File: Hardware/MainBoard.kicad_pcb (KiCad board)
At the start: 2 copper layers, 100 x 40 mm, 35 parts, among them J1 UPDI, J2 UART, J3 NMEA, J4 Vin, Q1 S8050, U1 HV5530, U2 HV5530, U3 ATtiny1606-S, U4 L78M05ABDT-TR

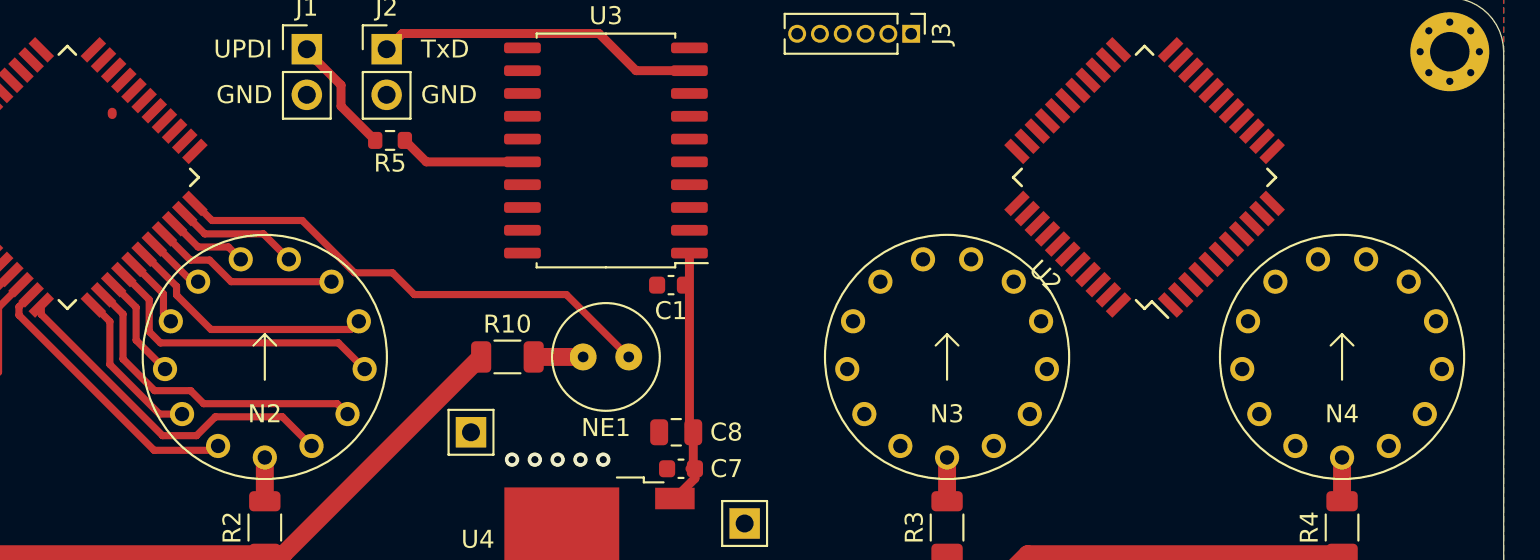
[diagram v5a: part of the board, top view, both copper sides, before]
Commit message: Routed right nixies
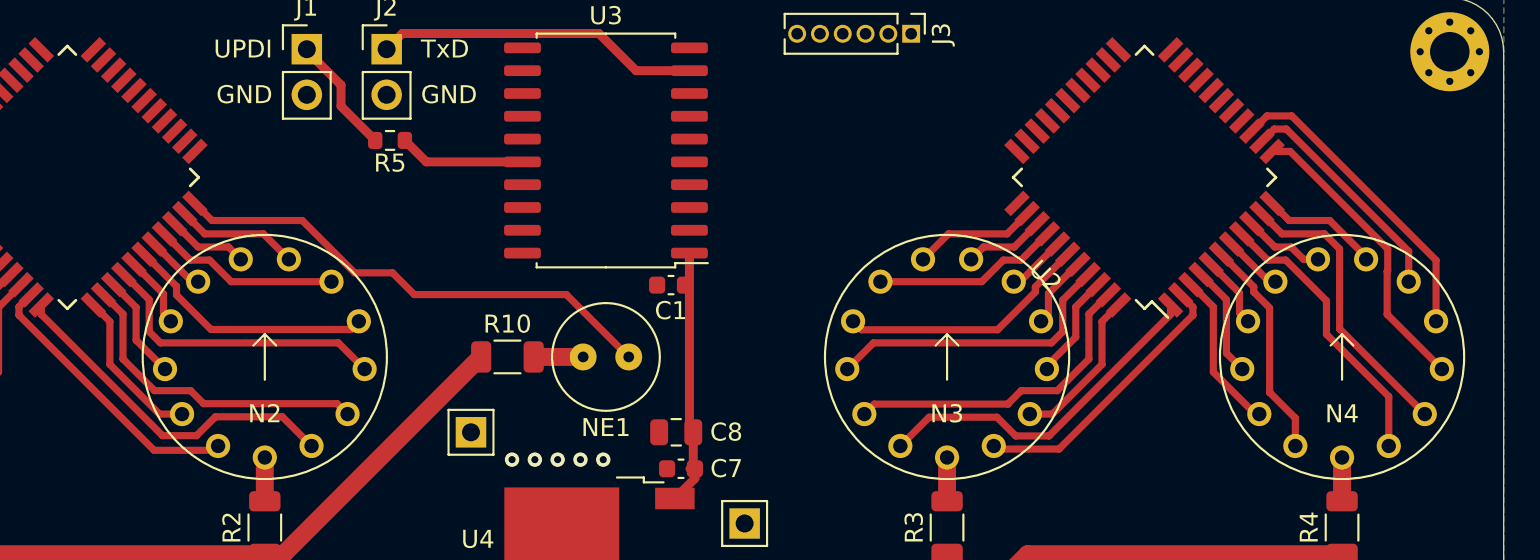
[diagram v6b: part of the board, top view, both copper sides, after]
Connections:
- U2 pad 1: /NixieTubes/N4_3 -> /NixieTubes/N3_L
- U2 pad 10: /NixieTubes/N3_7 -> /NixieTubes/N4_0
- U2 pad 11: /NixieTubes/N3_8 -> /NixieTubes/N4_6
- U2 pad 12: /NixieTubes/N3_9 -> /NixieTubes/N4_9
- U2 pad 13: /NixieTubes/N3_0 -> /NixieTubes/N4_7
- U2 pad 14: /NixieTubes/N3_R -> /NixieTubes/N4_8
- U2 pad 15: /NixieTubes/N3_L -> Net-(U2-Pad15)
- U2 pad 16: /NixieTubes/N3_1 -> Net-(U2-Pad16)
- U2 pad 17: /NixieTubes/N3_2 -> Net-(U2-Pad17)
- U2 pad 18: /NixieTubes/N3_3 -> Net-(U2-Pad18)
- U2 pad 2: /NixieTubes/N4_4 -> /NixieTubes/N3_R
- U2 pad 3: /NixieTubes/N4_5 -> /NixieTubes/N4_1
- U2 pad 35: Net-(U2-Pad35) -> /NixieTubes/N3_5
- U2 pad 36: Net-(U2-Pad36) -> /NixieTubes/N3_6
- U2 pad 37: Net-(U2-Pad37) -> /NixieTubes/N3_4
- U2 pad 38: /NixieTubes/N4_8 -> /NixieTubes/N3_7
- U2 pad 39: /NixieTubes/N4_9 -> /NixieTubes/N3_3
- U2 pad 4: /NixieTubes/N4_6 -> /NixieTubes/N4_2
- U2 pad 40: /NixieTubes/N4_0 -> /NixieTubes/N3_8
- U2 pad 41: /NixieTubes/N4_R -> /NixieTubes/N3_2
- U2 pad 42: /NixieTubes/N4_L -> /NixieTubes/N3_9
- U2 pad 43: /NixieTubes/N4_1 -> /NixieTubes/N3_1
- U2 pad 44: /NixieTubes/N4_2 -> /NixieTubes/N3_0
- U2 pad 5: /NixieTubes/N4_7 -> /NixieTubes/N4_3
- U2 pad 6: Net-(U2-Pad6) -> /NixieTubes/N4_L
- U2 pad 7: /NixieTubes/N3_4 -> /NixieTubes/N4_4
- U2 pad 8: /NixieTubes/N3_5 -> /NixieTubes/N4_R
- U2 pad 9: /NixieTubes/N3_6 -> /NixieTubes/N4_5
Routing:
- net /NixieTubes/N3_L: track 0.00 -> 19.5 mm
- net /NixieTubes/N3_1: track 0.00 -> 17.8 mm
- net /NixieTubes/N4_8: track 0.00 -> 17.3 mm
- net /NixieTubes/N4_9: track 0.00 -> 16.7 mm
- net /NixieTubes/N3_2: track 0.00 -> 16.6 mm
- net /NixieTubes/N4_0: track 0.00 -> 16.3 mm
- net /NixieTubes/N4_R: track 0.00 -> 15.8 mm
- net /NixieTubes/N3_R: track 0.00 -> 15.7 mm
- net /NixieTubes/N3_3: track 0.00 -> 14.1 mm
- net /NixieTubes/N4_7: track 0.00 -> 13.0 mm
- net /NixieTubes/N4_L: track 0.00 -> 12.4 mm
- net /NixieTubes/N3_4: track 0.00 -> 10.4 mm
- net /NixieTubes/N4_1: track 0.00 -> 8.92 mm
- net /NixieTubes/N3_0: track 0.00 -> 8.86 mm
- net /NixieTubes/N3_5: track 0.00 -> 6.86 mm
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
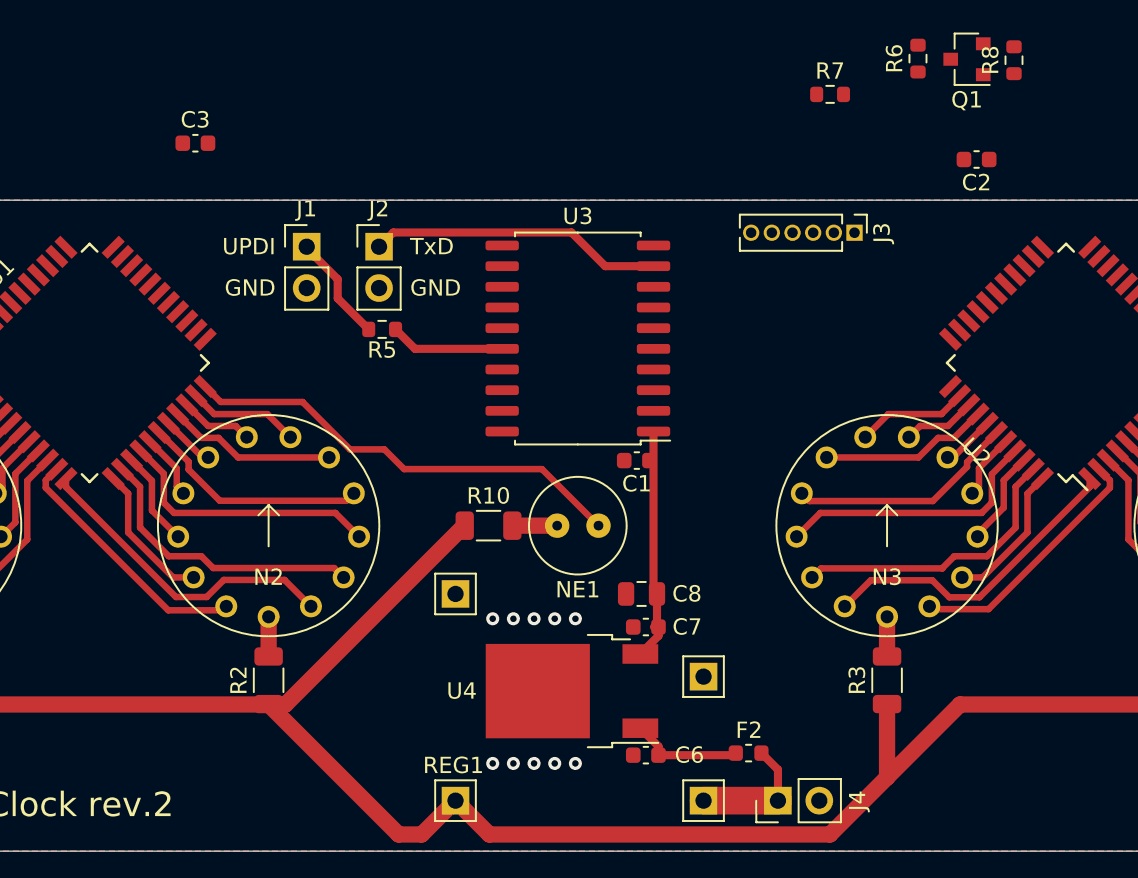
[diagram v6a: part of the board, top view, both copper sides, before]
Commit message: Finish routing connections
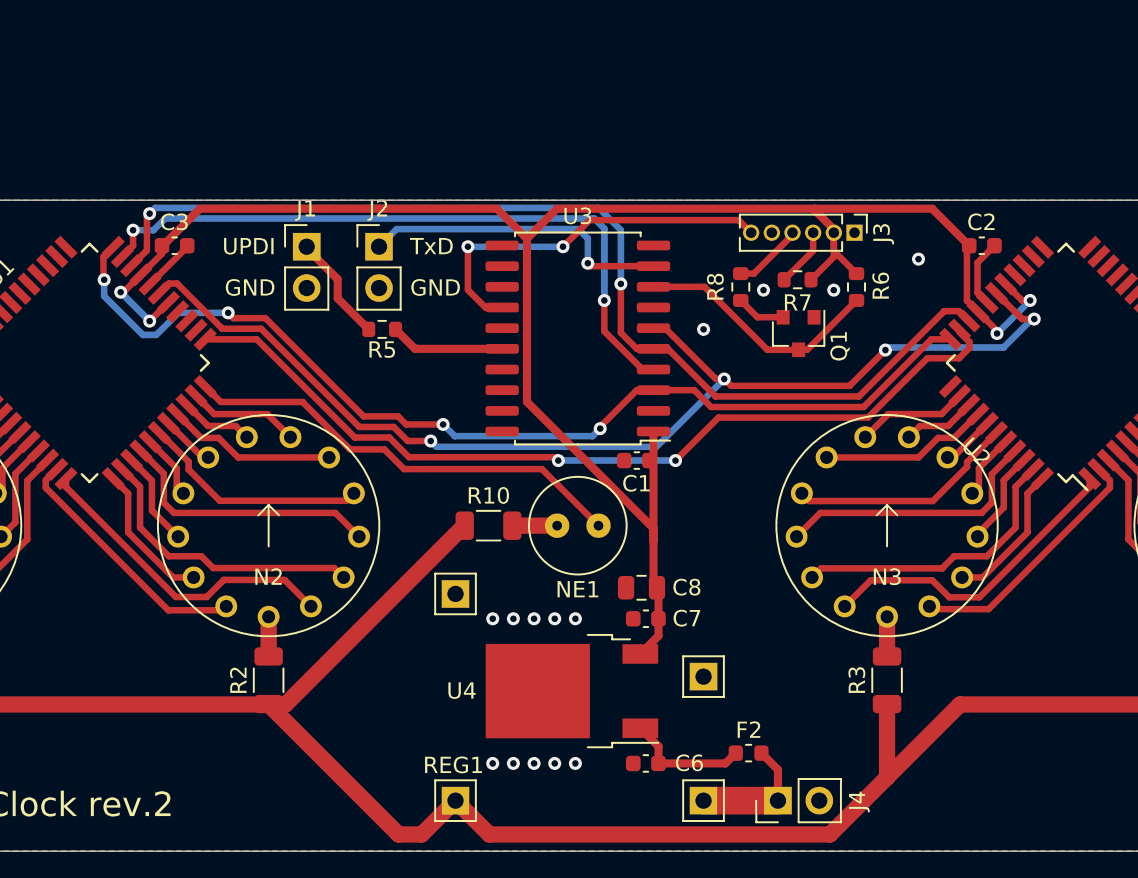
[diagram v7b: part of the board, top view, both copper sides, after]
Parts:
- moved R8 21.8 mm to (80.0, 25.3), turned to 270 degrees
- moved Q1 19.8 mm to (83.6, 28.2), turned to 270 degrees
- moved R6 14.5 mm to (87.1, 25.3), turned to 270 degrees
- moved R7 11.6 mm to (83.5, 24.9), turned to 180 degrees
- moved C3 6.43 mm to (45.2, 22.8)
- moved C2 5.31 mm to (94.8, 22.8), turned to 0 degrees
- moved C6 0.51 mm to (74.2, 54.6)
- moved C7 0.51 mm to (74.2, 45.7)
- moved C8 0.38 mm to (73.9, 43.8)
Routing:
- net +5V: track 14.3 -> 116.8 mm, vias 0 -> 4
- net NIX_CLK: track 0.00 -> 70.4 mm, vias 0 -> 4
- net NIX_LE: track 0.00 -> 65.1 mm, vias 0 -> 2
- net NIX_DIM: track 0.00 -> 64.0 mm, vias 0 -> 4
- net Net-(U1-Pad23): track 0.00 -> 54.2 mm, vias 0 -> 2
- net NIX_DATA: track 0.00 -> 41.7 mm, vias 0 -> 2
- net NMEA_SYNC: track 0.00 -> 23.6 mm, vias 0 -> 2
- net NMEA_RxD: track 0.00 -> 15.3 mm
- net GND: track 0.00 -> 7.47 mm, vias 10 -> 14
- net Net-(J3-Pad4): track 0.00 -> 4.30 mm
- net Net-(J3-Pad3): track 0.00 -> 3.63 mm
- net Net-(Q1-Pad2): track 0.00 -> 3.03 mm
- net UART_TxD: track 18.1 -> 19.2 mm, vias 0 -> 1
- net Net-(C6-Pad1): track 6.92 -> 7.82 mm

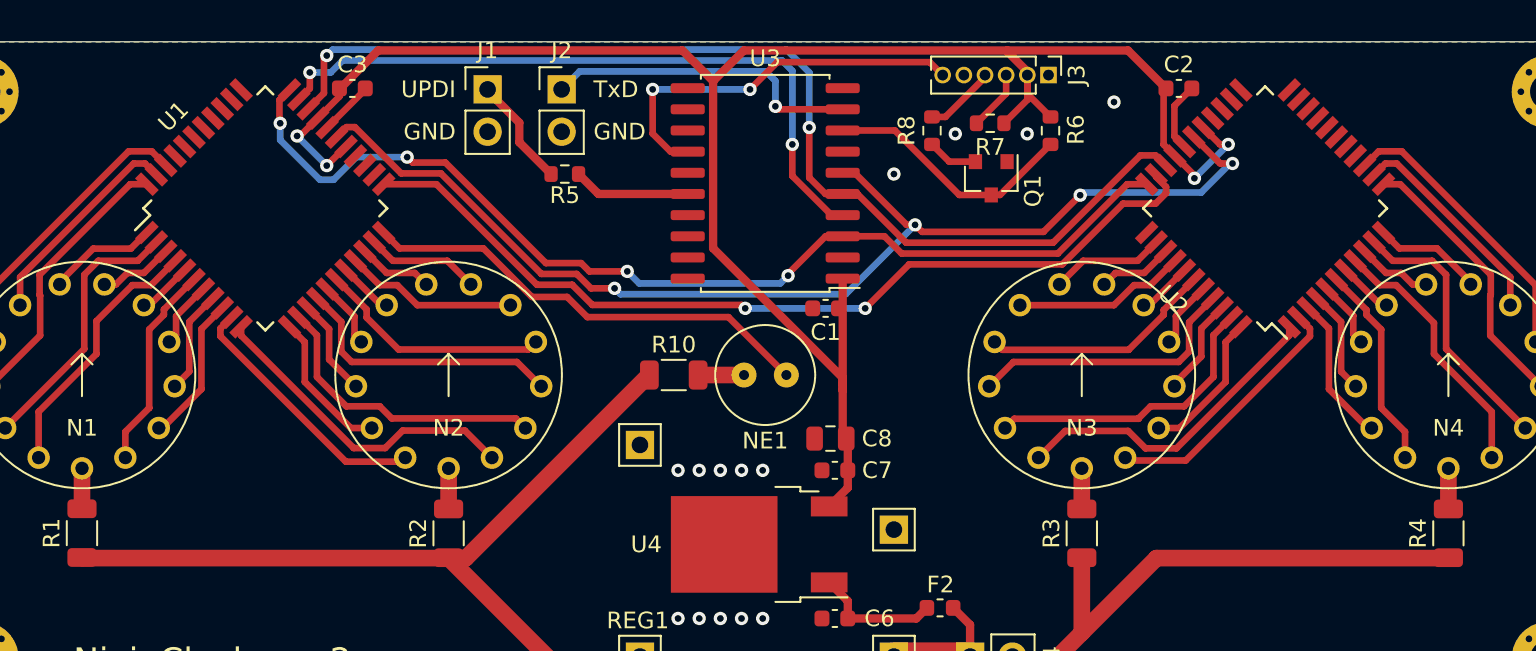
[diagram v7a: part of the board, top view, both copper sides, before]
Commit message: Add ground vias
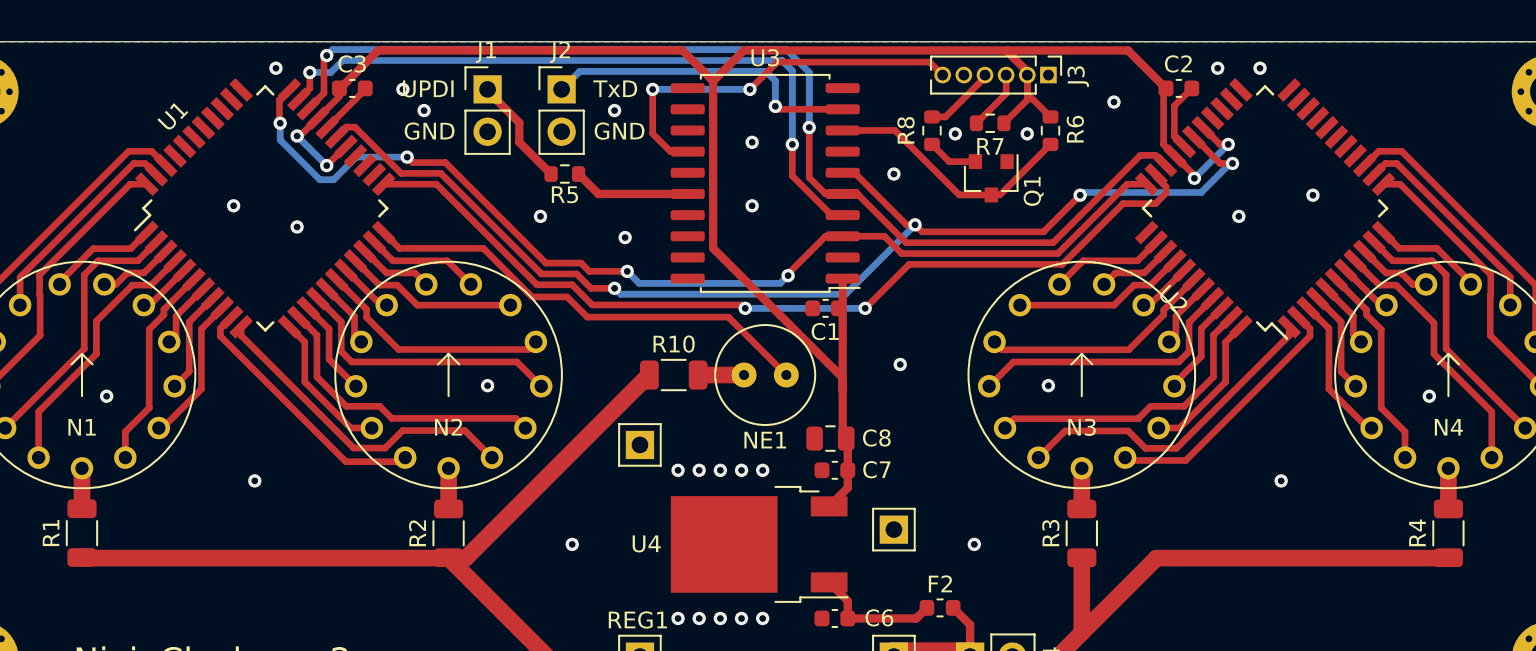
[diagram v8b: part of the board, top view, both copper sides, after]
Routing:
- net GND: vias 14 -> 37
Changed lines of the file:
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@@
     (thickness 1.6)
     (drawings 14)
-    (tracks 475)
+    (tracks 498)
     (zones 0)
     (modules 35)
@@
   (via (at 90.932 23.622) (size 0.8) (drill 0.4) (layers F.Cu B.Cu) (net 1))
   (via (at 77.724 27.94) (size 0.8) (drill 0.4) (layers F.Cu B.Cu) (net 1))
+  (via (at 69.215 26.035) (size 0.8) (drill 0.4) (layers F.Cu B.Cu) (net 1))
+  (via (at 69.215 29.845) (size 0.8) (drill 0.4) (layers F.Cu B.Cu) (net 1))
+  (via (at 61.595 31.75) (size 0.8) (drill 0.4) (layers F.Cu B.Cu) (net 1))
+  (via (at 56.515 30.48) (size 0.8) (drill 0.4) (layers F.Cu B.Cu) (net 1))
+  (via (at 60.96 24.13) (size 0.8) (drill 0.4) (layers F.Cu B.Cu) (net 1))
+  (via (at 49.53 24.13) (size 0.8) (drill 0.4) (layers F.Cu B.Cu) (net 1))
+  (via (at 38.1 29.845) (size 0.8) (drill 0.4) (layers F.Cu B.Cu) (net 1))
+  (via (at 41.91 31.115) (size 0.8) (drill 0.4) (layers F.Cu B.Cu) (net 1))
+  (via (at 98.425 30.48) (size 0.8) (drill 0.4) (layers F.Cu B.Cu) (net 1))
+  (via (at 102.87 29.21) (size 0.8) (drill 0.4) (layers F.Cu B.Cu) (net 1))
+  (via (at 109.855 41.275) (size 0.8) (drill 0.4) (layers F.Cu B.Cu) (net 1))
+  (via (at 86.995 40.64) (size 0.8) (drill 0.4) (layers F.Cu B.Cu) (net 1))
+  (via (at 53.34 40.64) (size 0.8) (drill 0.4) (layers F.Cu B.Cu) (net 1))
+  (via (at 30.48 41.275) (size 0.8) (drill 0.4) (layers F.Cu B.Cu) (net 1))
+  (via (at 39.37 46.355) (size 0.8) (drill 0.4) (layers F.Cu B.Cu) (net 1))
+  (via (at 100.965 46.355) (size 0.8) (drill 0.4) (layers F.Cu B.Cu) (net 1))
+  (via (at 82.55 50.165) (size 0.8) (drill 0.4) (layers F.Cu B.Cu) (net 1))
+  (via (at 78.105 39.37) (size 0.8) (drill 0.4) (layers F.Cu B.Cu) (net 1))
+  (via (at 58.42 50.165) (size 0.8) (drill 0.4) (layers F.Cu B.Cu) (net 1))
+  (via (at 99.695 21.59) (size 0.8) (drill 0.4) (layers F.Cu B.Cu) (net 1))
+  (via (at 40.64 21.59) (size 0.8) (drill 0.4) (layers F.Cu B.Cu) (net 1))
+  (via (at 48.26 22.86) (size 0.8) (drill 0.4) (layers F.Cu B.Cu) (net 1))
+  (via (at 97.155 21.59) (size 0.8) (drill 0.4) (layers F.Cu B.Cu) (net 1))
   (via (at 70.612 23.876) (size 0.8) (drill 0.4) (layers F.Cu B.Cu) (net 78))
   (via (at 88.9 29.21) (size 0.8) (drill 0.4) (layers F.Cu B.Cu) (net 76))
